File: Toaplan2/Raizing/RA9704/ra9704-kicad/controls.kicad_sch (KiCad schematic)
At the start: 9 parts, among them U310 RE9511, U311 M54532P, U320 74HC240, U321 74HC240, U322 74HC240, U331 74HC174, U34 RE9511, U38 RE9511, U39 RE9511

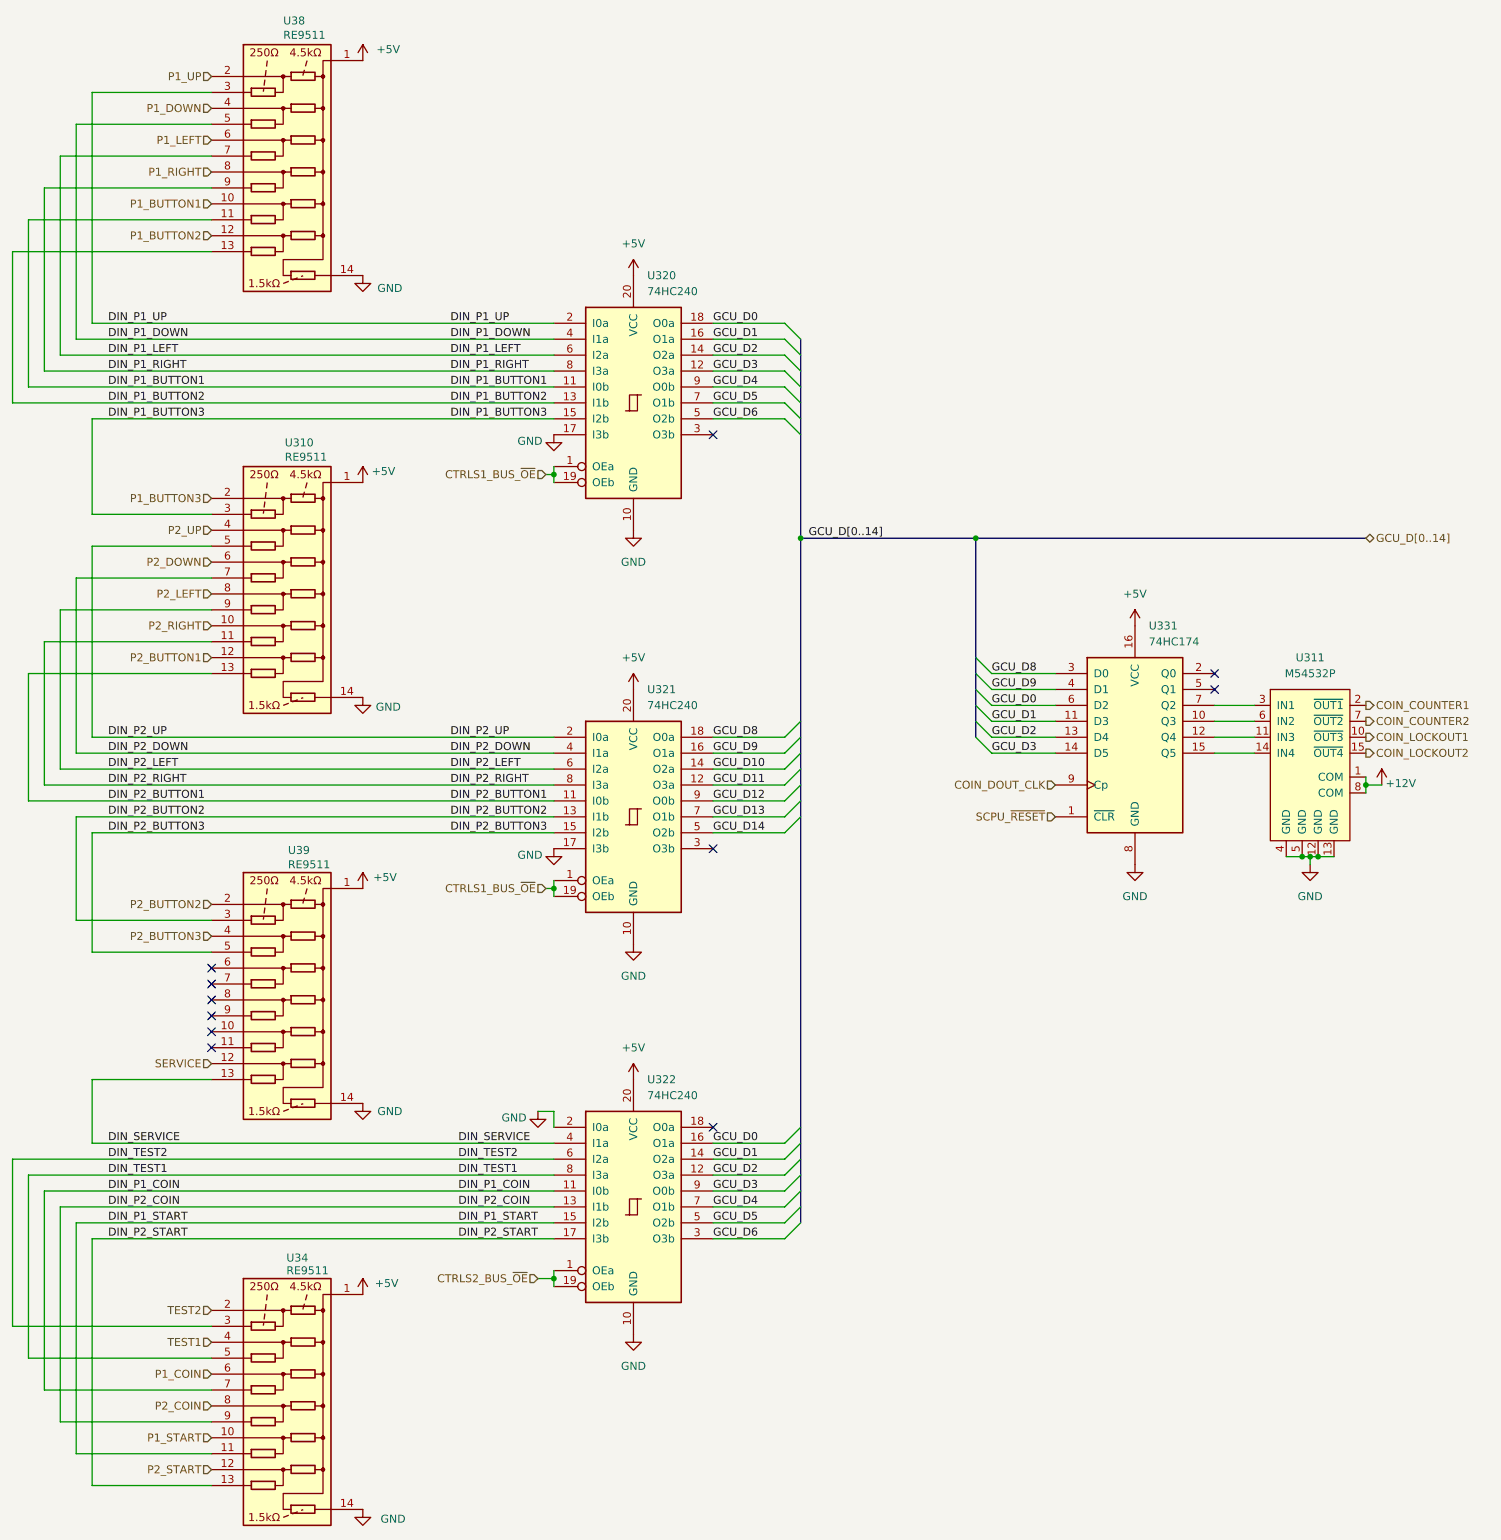
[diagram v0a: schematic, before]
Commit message: fix(ra9704): Add Os as a proxy for 0s in all reference designators
RA9704 has reference designators such that each number has a preceding zero (e.g. RA076, U074, etc.). This causes a bug in KiCAD.

This is 'fixed' by using the 'O' (the letter 'Oh') character instead.

For more info, see the following issue on the KiCAD Gitlab repo

https://gitlab.com/kicad/code/kicad/-/issues/19229
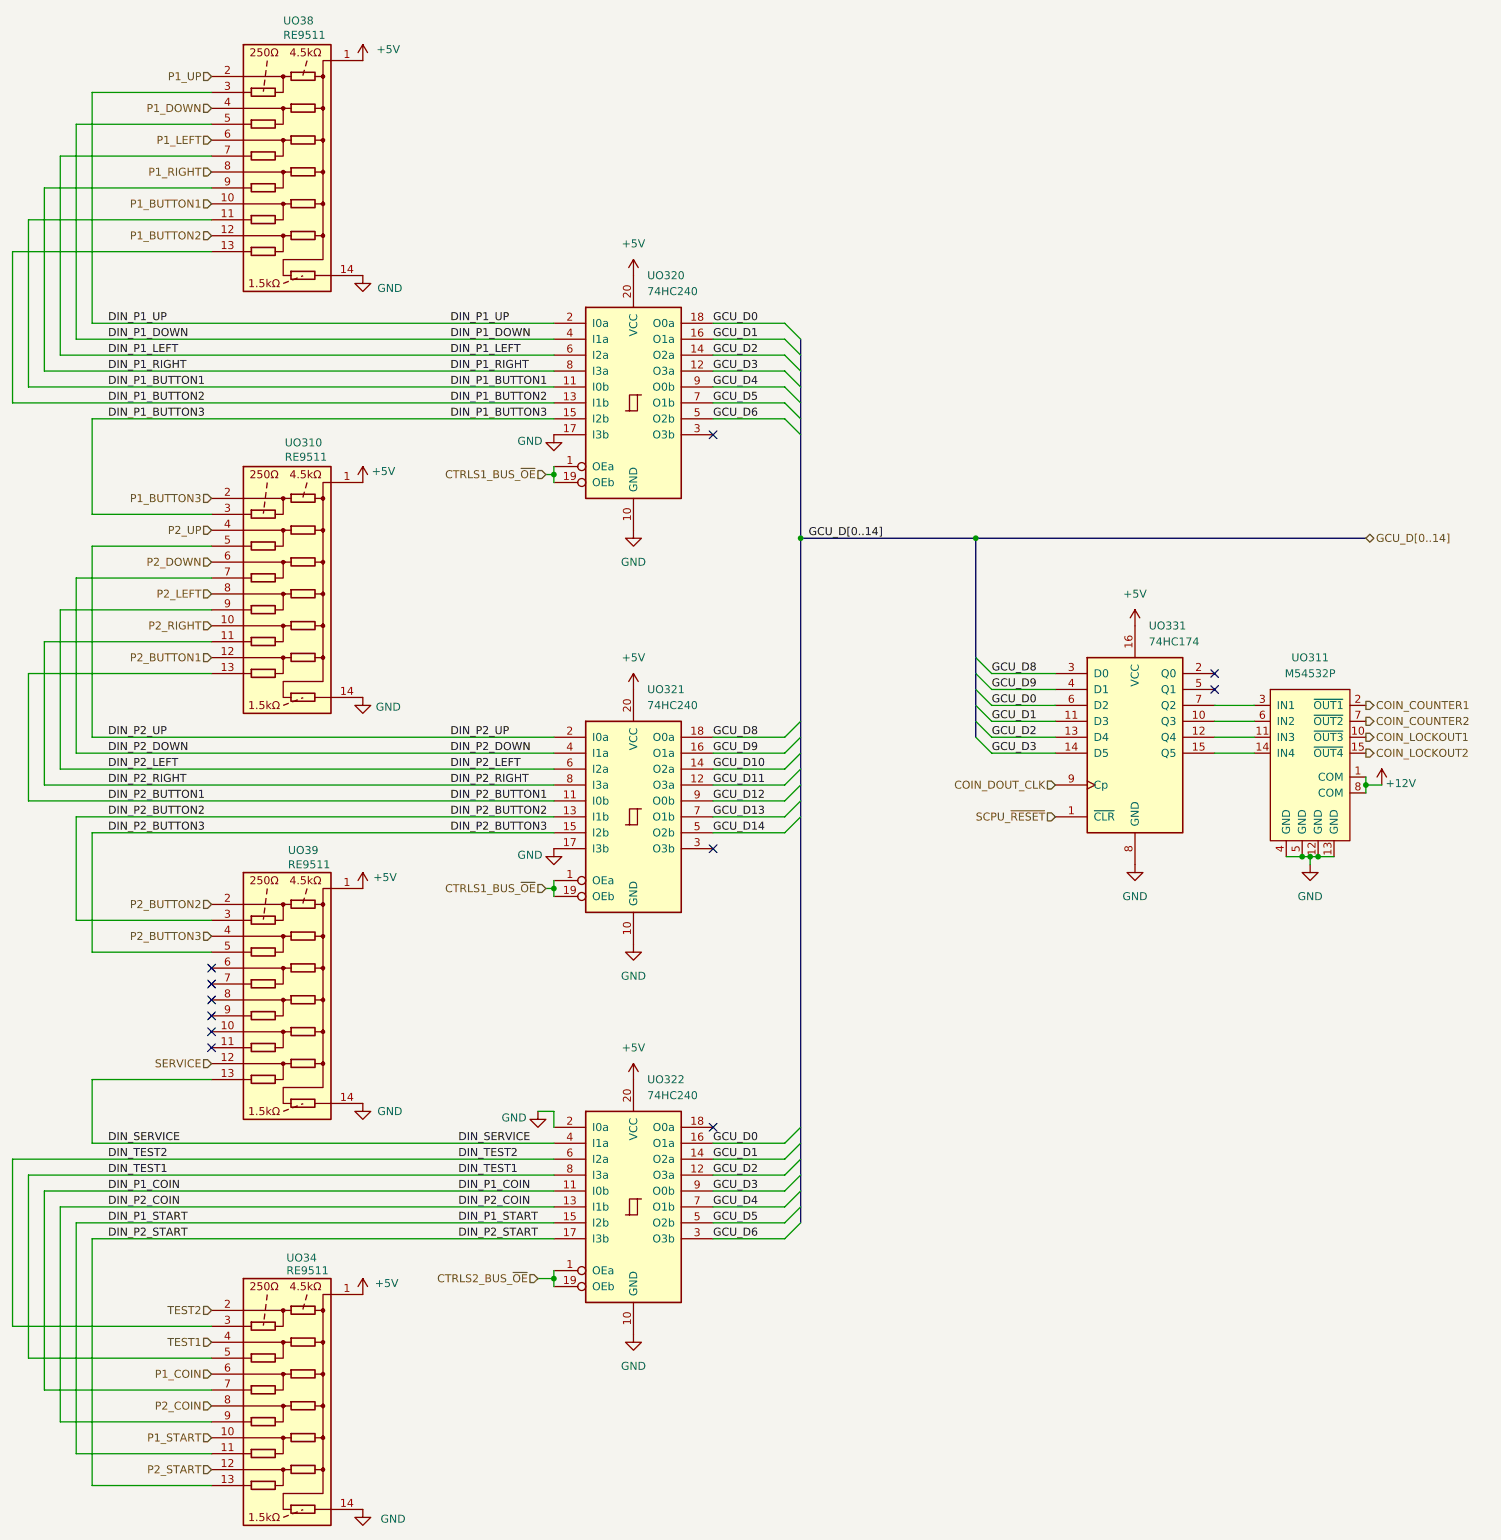
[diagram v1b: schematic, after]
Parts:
- renumbered U310 to UO310, U311 to UO311, U320 to UO320, U321 to UO321, U322 to UO322, U331 to UO331, U34 to UO34, U38 to UO38, U39 to UO39
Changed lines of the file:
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@@
 		(dnp no)
 		(fields_autoplaced yes)
-		(property "Reference" "U322"
+		(property "Reference" "UO322"
 			(at 221.9041 185.42 0)
 			(effects
@@
 			(project "ra9704"
 				(path "/24d3b4cf-2360-45fc-8c40-cedc8afdf9e1/fff27fdf-780e-4580-8f2a-71b69cb8c7b9"
-					(reference "U322")
+					(reference "UO322")
 					(unit 1)
 				)
@@
 		(dnp no)
 		(fields_autoplaced yes)
-		(property "Reference" "U331"
+		(property "Reference" "UO331"
 			(at 301.9141 113.03 0)
 			(effects
@@
 			(project "ra9704"
 				(path "/24d3b4cf-2360-45fc-8c40-cedc8afdf9e1/fff27fdf-780e-4580-8f2a-71b69cb8c7b9"
-					(reference "U331")
+					(reference "UO331")
 					(unit 1)
 				)
@@
 		(dnp no)
 		(fields_autoplaced yes)
-		(property "Reference" "U311"
+		(property "Reference" "UO311"
 			(at 327.66 118.11 0)
 			(effects
@@
 			(project "ra9704"
 				(path "/24d3b4cf-2360-45fc-8c40-cedc8afdf9e1/fff27fdf-780e-4580-8f2a-71b69cb8c7b9"
-					(reference "U311")
+					(reference "UO311")
 					(unit 1)
 				)
@@
 		(on_board yes)
 		(dnp no)
-		(property "Reference" "U39"
+		(property "Reference" "UO39"
 			(at 164.592 148.844 0)
 			(effects
@@
 			(project "ra9704"
 				(path "/24d3b4cf-2360-45fc-8c40-cedc8afdf9e1/fff27fdf-780e-4580-8f2a-71b69cb8c7b9"
-					(reference "U39")
+					(reference "UO39")
 					(unit 1)
 				)
@@
 		(dnp no)
 		(fields_autoplaced yes)
-		(property "Reference" "U320"
+		(property "Reference" "UO320"
 			(at 221.9041 57.15 0)
 			(effects
@@
 			(project "ra9704"
 				(path "/24d3b4cf-2360-45fc-8c40-cedc8afdf9e1/fff27fdf-780e-4580-8f2a-71b69cb8c7b9"
-					(reference "U320")
+					(reference "UO320")
 					(unit 1)
 				)
@@
 		(on_board yes)
 		(dnp no)
-		(property "Reference" "U310"
+		(property "Reference" "UO310"
 			(at 164.084 83.82 0)
 			(effects
@@
 			(project "ra9704"
 				(path "/24d3b4cf-2360-45fc-8c40-cedc8afdf9e1/fff27fdf-780e-4580-8f2a-71b69cb8c7b9"
-					(reference "U310")
+					(reference "UO310")
 					(unit 1)
 				)
@@
 		(dnp no)
 		(fields_autoplaced yes)
-		(property "Reference" "U321"
+		(property "Reference" "UO321"
 			(at 221.9041 123.19 0)
 			(effects
@@
 			(project "ra9704"
 				(path "/24d3b4cf-2360-45fc-8c40-cedc8afdf9e1/fff27fdf-780e-4580-8f2a-71b69cb8c7b9"
-					(reference "U321")
+					(reference "UO321")
 					(unit 1)
 				)
@@
 		(on_board yes)
 		(dnp no)
-		(property "Reference" "U34"
+		(property "Reference" "UO34"
 			(at 164.338 213.868 0)
 			(effects
@@
 			(project "ra9704"
 				(path "/24d3b4cf-2360-45fc-8c40-cedc8afdf9e1/fff27fdf-780e-4580-8f2a-71b69cb8c7b9"
-					(reference "U34")
+					(reference "UO34")
 					(unit 1)
 				)
@@
 		(on_board yes)
 		(dnp no)
-		(property "Reference" "U38"
+		(property "Reference" "UO38"
 			(at 163.83 16.51 0)
 			(effects
@@
 			(project "ra9704"
 				(path "/24d3b4cf-2360-45fc-8c40-cedc8afdf9e1/fff27fdf-780e-4580-8f2a-71b69cb8c7b9"
-					(reference "U38")
-					(unit 1)
-				)
+					(reference "UO38")
+					(unit 1)
+				)
